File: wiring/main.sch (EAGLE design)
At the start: 39 parts, among them IC1 attiny 2313A, J2 J7MM, J3 J5MM, J4 J10MM, J5 J7MM, J7 J5MM, Q1 12MHz, X1 USB-B

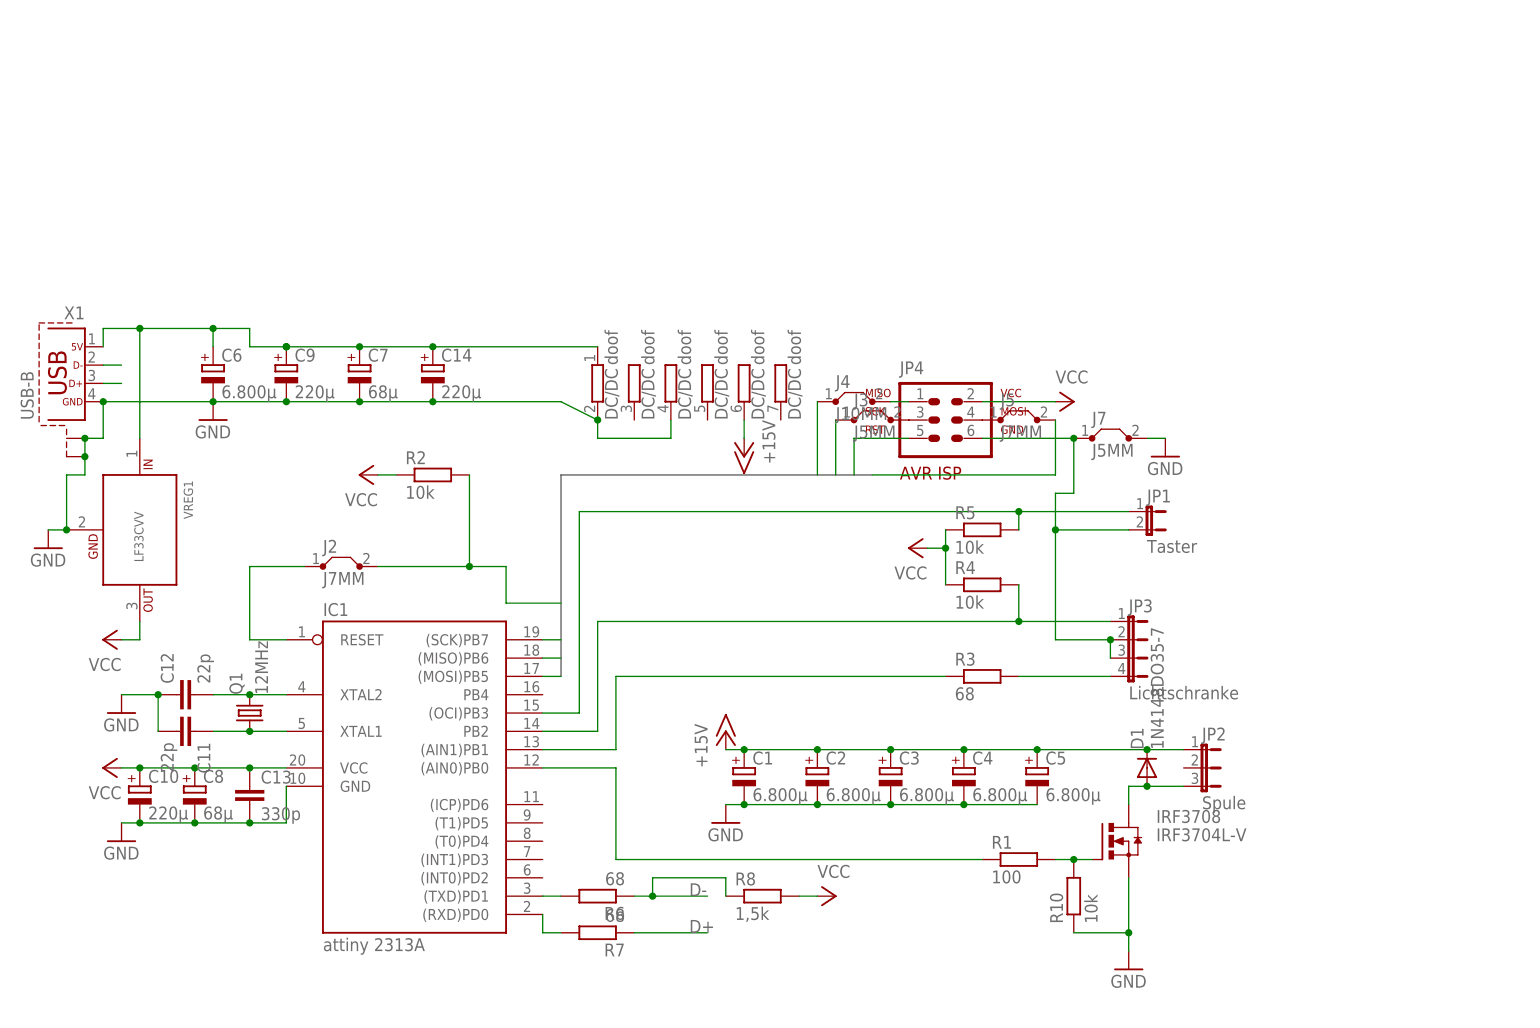
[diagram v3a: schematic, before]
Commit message: schaltplan überarbeitet
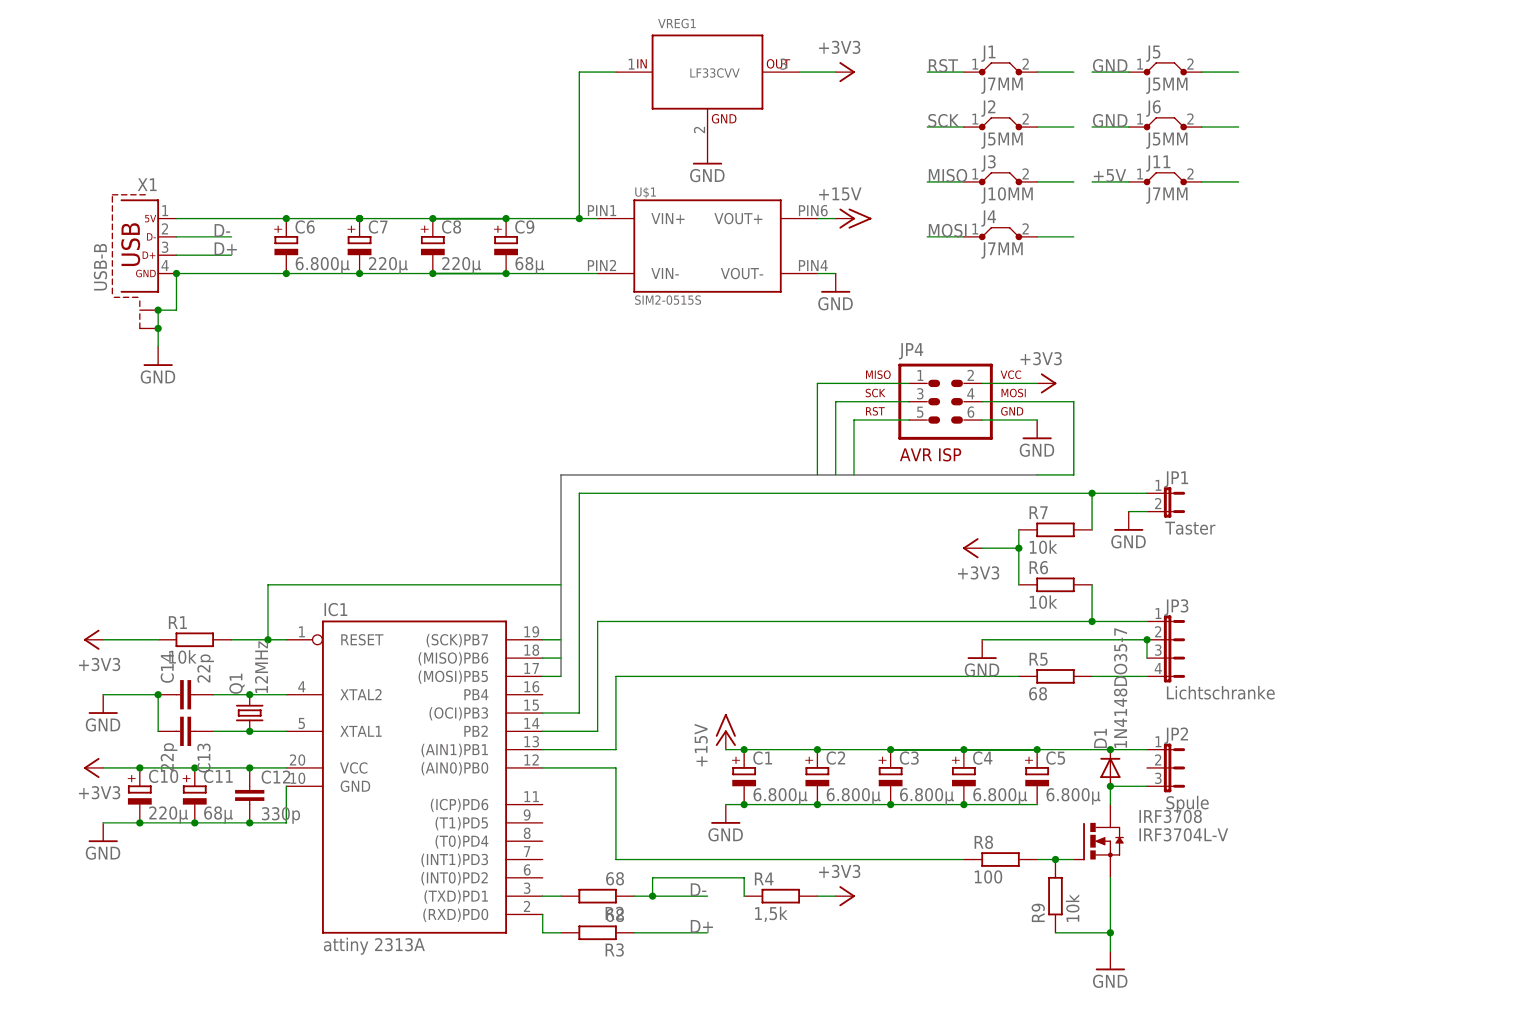
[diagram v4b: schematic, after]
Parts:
- removed DC/DC: doof, resistor-sil:GE06RP
- removed J7: J5MM, jumper:J5MM
- removed R10: 10k, rcl:R-EU_0207/10
- added J1, J11: J7MM, jumper:J7MM
- added J6: J5MM, jumper:J5MM
- added R9: 10k, rcl:R-EU_0207/10
- added U$1: SIM2-0515S, eigene:SIM2-0515S
- C11: value 22p -> 68µ; device rcl:C-EU050-024X044 -> resistor:CPOL-EUE2.5-7
- C12: value 22p -> 330p
- C13: value 330p -> 22p
- C14: value 220µ -> 22p; device resistor:CPOL-EUE2.5-7 -> rcl:C-EU050-024X044
- C7, C8: value 68µ -> 220µ
- C9: value 220µ -> 68µ
- J2, J5: value J7MM -> J5MM; device jumper:J7MM -> jumper:J5MM
- J3: value J5MM -> J10MM; device jumper:J5MM -> jumper:J10MM
- J4: value J10MM -> J7MM; device jumper:J10MM -> jumper:J7MM
- R1: value 100 -> 10k
- R2, R5: value 10k -> 68
- R4: value 10k -> 1,5k
- R6, R7: value 68 -> 10k
- R8: value 1,5k -> 100
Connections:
- removed net 5V: C14.+, C6.+, C7.+, C9.+, DC/DCA.1, VREG1.IN, X1.1
- removed net N$1: IC1.RESET, J2.1
- removed net N$10: J4.2, JP4.1
- removed net N$20: J5.1, JP4.4
- removed net N$22: J7.1, JP1.2, JP3.2, JP3.3, JP4.6
- removed net N$9: J3.2, JP4.3
- removed net RST1: J2.2, JP4.5, R2.2
- new net +5V: C6.+, C7.+, C8.+, C9.+, J11.1, J11.2, U$1.VIN+, VREG1.IN, X1.1
- new net RST: IC1.RESET, J1.1, J1.2, JP4.5, R1.2
- net +15V: now also U$1.VOUT+; no longer DC/DCE.2
- net D+: now also R3.1; no longer R7.1
- net D-: now also R2.1, R4.1; no longer R6.1, R8.1
- net GND: now also C11.-, C12.2, C14.1, J5.1, J5.2, J6.1, J6.2, JP1.2, JP3.2, JP3.3, JP4.6, R9.1, U$1.VIN-, U$1.VOUT-; no longer C11.2, C12.1, C14.-, DC/DCA.2, DC/DCC.2, J7.2, R10.1
- net MISO: now also J3.1, J3.2, JP4.1; no longer J4.1
- net MOSI: now also J4.1, J4.2, JP4.4; no longer J5.2
- net N$11: now also C13.1; no longer C11.1
- net N$12: now also C14.2; no longer C12.2
- net N$13: now also R7.2; no longer R5.2
- net N$14: now also R5.1; no longer R3.1
- net N$15: now also R6.2; no longer R4.2
- net N$18: now also R3.2; no longer R7.2
- net N$19: now also R2.2; no longer R6.2
- net N$2: now also R8.2, R9.2; no longer R1.2, R10.2
- net N$8: now also R5.2; no longer R3.2
- net PB0: now also R8.1; no longer R1.1
- net SCK: now also J2.1, J2.2, JP4.3; no longer J3.1
- net VCC: now also C11.+, C12.1, R1.1, R4.2, R6.1, R7.1; no longer C13.1, C8.+, R2.1, R4.1, R5.1, R8.2
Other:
- moved on the sheet: C12, C13, C6, C7, C8, C9, D1, IRF3708, J2, J3, J4, J5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

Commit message: wiring power led eingezeichnet
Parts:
- added LED1, LED2: (no value), led:LED3MM
- added LED3: LED 3MM 2MA GN, led:LED3MM
- added R10: 649, rcl:R-EU_0207/7
- added R11: 1,5k, rcl:R-EU_0207/7
- added R12: 6,49k, rcl:R-EU_0207/10
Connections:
- removed net VCC: C10.+, C11.+, C12.1, IC1.VCC, JP4.2, R1.1, R4.2, R6.1, R7.1, VREG1.OUT
- new net +3V3: C10.+, C11.+, C12.1, IC1.VCC, JP4.2, LED1.A, R1.1, R4.2, R6.1, R7.1, VREG1.OUT
- new net N$1: LED3.C, R12.1
- new net N$4: LED2.C, R11.1
- new net N$5: LED1.C, R10.1
- net +15V: now also LED3.A
- net +5V: now also LED2.A
- net GND: now also R10.2, R11.2, R12.2

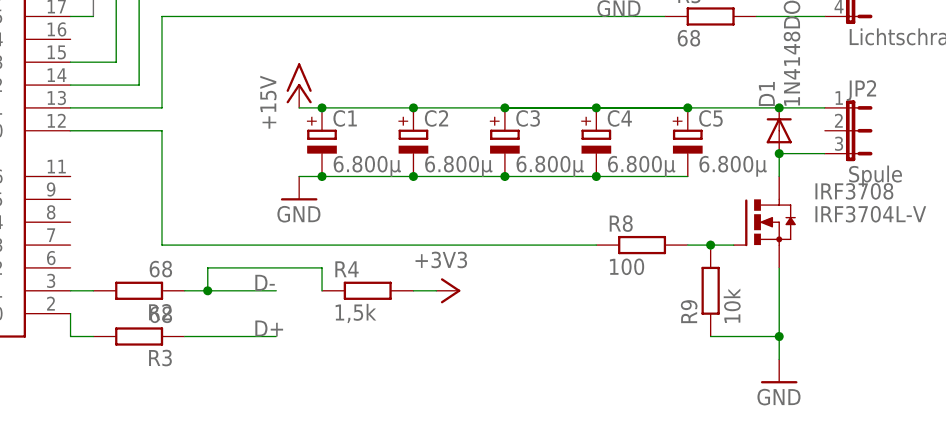
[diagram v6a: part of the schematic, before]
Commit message: wiring schaltazeige led eingezeichnet
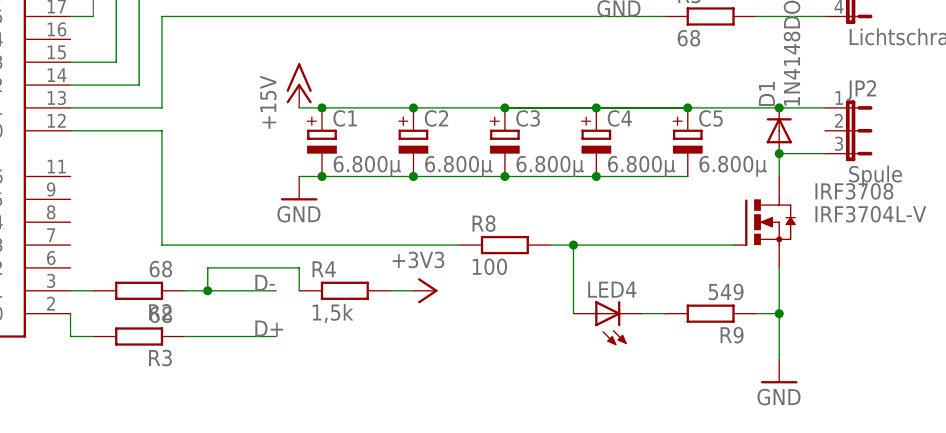
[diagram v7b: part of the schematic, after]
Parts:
- added LED4: (no value), led:LED3MM
- R9: value 10k -> 549
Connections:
- new net N$6: LED4.C, R9.2
- net N$2: now also LED4.A; no longer R9.2
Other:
- moved on the sheet: R4, R8, R9
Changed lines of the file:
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@@
 <part name="D1" library="diode" deviceset="1N4148" device="DO35-7"/>
 <part name="IRF3708" library="transistor-power" deviceset="IRF3704" device="L-V"/>
-<part name="R9" library="rcl" deviceset="R-EU_" device="0207/10" value="10k"/>
+<part name="R9" library="rcl" deviceset="R-EU_" device="0207/10" value="549"/>
 <part name="C8" library="resistor" deviceset="CPOL-EU" device="E2.5-7" value="220µ"/>
 <part name="P+5" library="supply1" deviceset="+15V" device=""/>
@@
 <part name="P+11" library="supply1" deviceset="+5V" device=""/>
 <part name="P+12" library="supply1" deviceset="+5V" device=""/>
+<part name="LED4" library="led" deviceset="LED" device="3MM"/>
 </parts>
 <sheets>
@@
 <instance part="C7" gate="G$1" x="17.78" y="109.22"/>
 <instance part="C10" gate="G$1" x="-12.7" y="33.02"/>
-<instance part="R8" gate="G$1" x="106.68" y="22.86"/>
+<instance part="R8" gate="G$1" x="91.44" y="22.86"/>
 <instance part="R1" gate="G$1" x="-5.08" y="53.34"/>
 <instance part="C13" gate="G$1" x="-5.08" y="40.64" rot="R270"/>
@@
 <instance part="R2" gate="G$1" x="50.8" y="17.78" rot="R180"/>
 <instance part="R3" gate="G$1" x="50.8" y="12.7" rot="R180"/>
-<instance part="R4" gate="G$1" x="76.2" y="17.78"/>
+<instance part="R4" gate="G$1" x="73.66" y="17.78"/>
 <instance part="JP4" gate="G$1" x="99.06" y="86.36"/>
 <instance part="P+2" gate="G$1" x="101.6" y="66.04" rot="R90"/>
-<instance part="P+3" gate="G$1" x="86.36" y="17.78" rot="R270"/>
+<instance part="P+3" gate="G$1" x="83.82" y="17.78" rot="R270"/>
 <instance part="P+4" gate="G$1" x="114.3" y="88.9" rot="R270"/>
 <instance part="P+1" gate="G$1" x="-20.32" y="35.56" rot="R90"/>
@@
 <instance part="D1" gate="G$1" x="121.92" y="35.56" rot="R90"/>
 <instance part="IRF3708" gate="G$1" x="119.38" y="25.4"/>
-<instance part="R9" gate="G$1" x="114.3" y="17.78" rot="R90"/>
+<instance part="R9" gate="G$1" x="114.3" y="15.24" rot="R180"/>
 <instance part="C8" gate="G$1" x="27.94" y="109.22"/>
 <instance part="P+5" gate="1" x="86.36" y="111.76" rot="R270"/>
@@
 <instance part="P+11" gate="1" x="162.56" y="119.38"/>
 <instance part="P+12" gate="1" x="7.62" y="119.38"/>
+<instance part="LED4" gate="G$1" x="101.6" y="15.24" rot="R90"/>
 </instances>
 <busses>
@@
 <segment>
 <pinref part="R8" gate="G$1" pin="2"/>
-<wire x1="111.76" y1="22.86" x2="114.3" y2="22.86" width="0.1524" layer="91"/>
-<pinref part="R9" gate="G$1" pin="2"/>
 <pinref part="IRF3708" gate="G$1" pin="G"/>
-<wire x1="114.3" y1="22.86" x2="116.84" y2="22.86" width="0.1524" layer="91"/>
-<junction x="114.3" y="22.86"/>
+<wire x1="96.52" y1="22.86" x2="99.06" y2="22.86" width="0.1524" layer="91"/>
+<pinref part="LED4" gate="G$1" pin="A"/>
+<wire x1="99.06" y1="22.86" x2="116.84" y2="22.86" width="0.1524" layer="91"/>
+<wire x1="99.06" y1="15.24" x2="99.06" y2="22.86" width="0.1524" layer="91"/>
+<junction x="99.06" y="22.86"/>
 </segment>
 </net>
@@
 <segment>
 <pinref part="R8" gate="G$1" pin="1"/>
-<wire x1="101.6" y1="22.86" x2="53.34" y2="22.86" width="0.1524" layer="91"/>
+<wire x1="86.36" y1="22.86" x2="53.34" y2="22.86" width="0.1524" layer="91"/>
 <pinref part="IC1" gate="G$1" pin="(AIN0)PB0"/>
 <wire x1="53.34" y1="22.86" x2="53.34" y2="35.56" width="0.1524" layer="91"/>
@@
 <pinref part="IRF3708" gate="G$1" pin="S"/>
 <pinref part="R9" gate="G$1" pin="1"/>
-<wire x1="121.92" y1="10.16" x2="121.92" y2="12.7" width="0.1524" layer="91"/>
-<wire x1="121.92" y1="12.7" x2="121.92" y2="20.32" width="0.1524" layer="91"/>
-<wire x1="114.3" y1="12.7" x2="121.92" y2="12.7" width="0.1524" layer="91"/>
-<junction x="121.92" y="12.7"/>
+<wire x1="121.92" y1="10.16" x2="121.92" y2="15.24" width="0.1524" layer="91"/>
+<wire x1="121.92" y1="15.24" x2="121.92" y2="20.32" width="0.1524" layer="91"/>
+<wire x1="119.38" y1="15.24" x2="121.92" y2="15.24" width="0.1524" layer="91"/>
+<junction x="121.92" y="15.24"/>
 </segment>
 <segment>
@@
 <wire x1="58.42" y1="17.78" x2="55.88" y2="17.78" width="0.1524" layer="91"/>
 <wire x1="58.42" y1="17.78" x2="58.42" y2="20.32" width="0.1524" layer="91"/>
-<wire x1="58.42" y1="20.32" x2="71.12" y2="20.32" width="0.1524" layer="91"/>
+<wire x1="58.42" y1="20.32" x2="68.58" y2="20.32" width="0.1524" layer="91"/>
 <pinref part="R4" gate="G$1" pin="1"/>
-<wire x1="71.12" y1="20.32" x2="71.12" y2="17.78" width="0.1524" layer="91"/>
+<wire x1="68.58" y1="20.32" x2="68.58" y2="17.78" width="0.1524" layer="91"/>
 <junction x="58.42" y="17.78"/>
 <label x="63.5" y="17.78" size="1.778" layer="95"/>
@@
 <pinref part="R4" gate="G$1" pin="2"/>
 <pinref part="P+3" gate="G$1" pin="+3V3"/>
-<wire x1="83.82" y1="17.78" x2="81.28" y2="17.78" width="0.1524" layer="91"/>
+<wire x1="81.28" y1="17.78" x2="78.74" y2="17.78" width="0.1524" layer="91"/>
 </segment>
 <segment>
@@
 </segment>
 </net>
+<net name="N$6" class="0">
+<segment>
+<pinref part="R9" gate="G$1" pin="2"/>
+<pinref part="LED4" gate="G$1" pin="C"/>
+<wire x1="106.68" y1="15.24" x2="109.22" y2="15.24" width="0.1524" layer="91"/>
+</segment>
+</net>
